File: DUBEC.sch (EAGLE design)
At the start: 69 parts

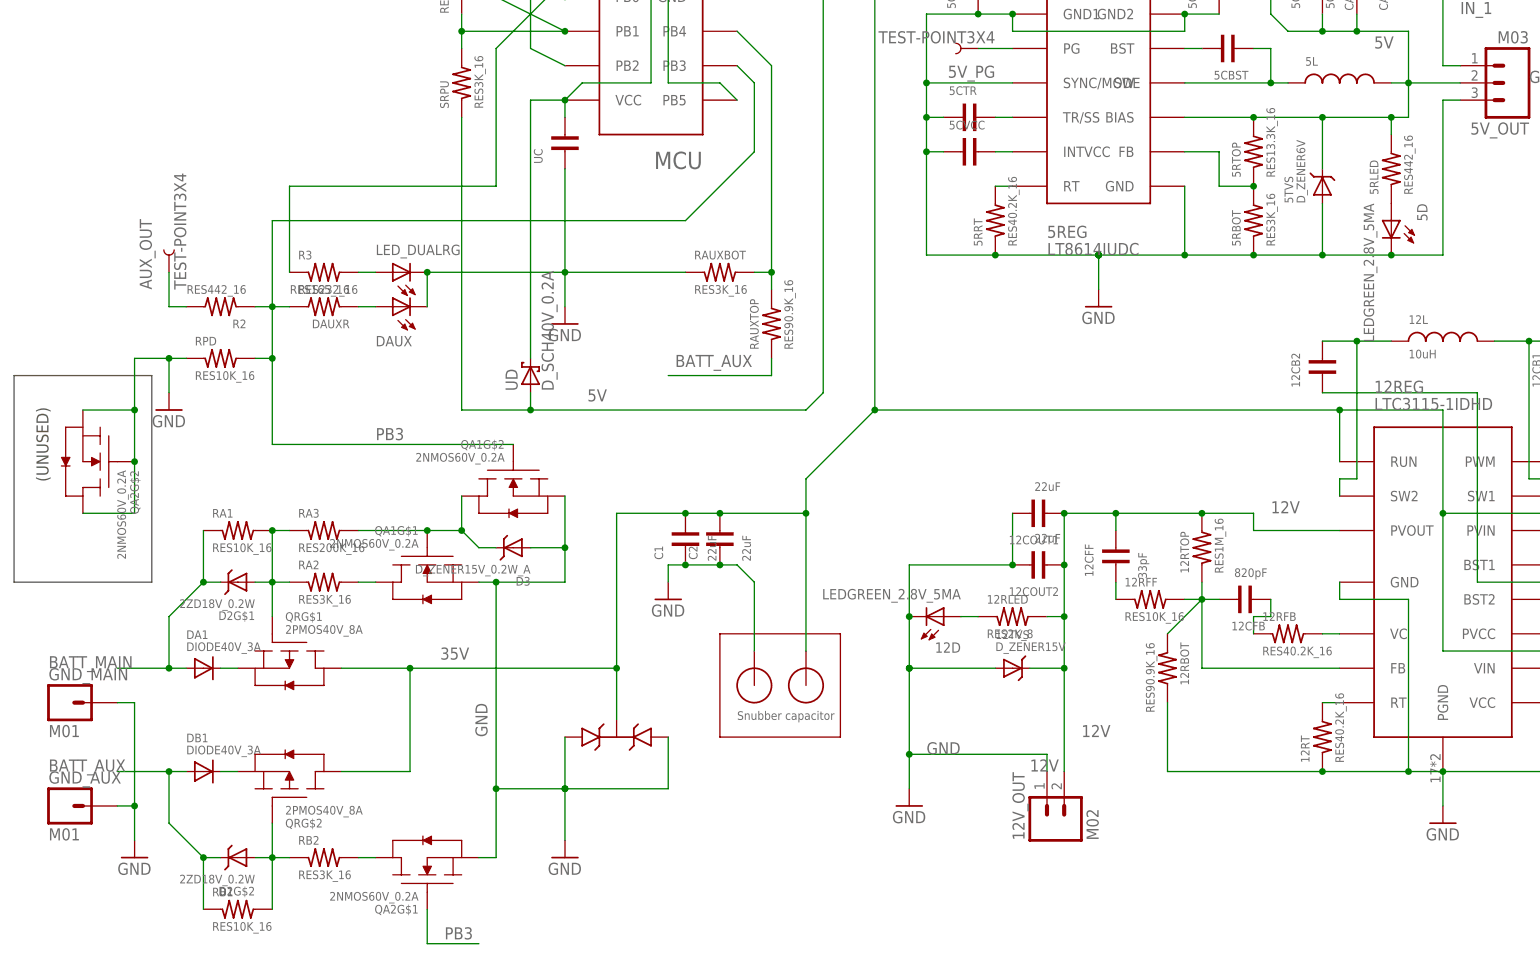
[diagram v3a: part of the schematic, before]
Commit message: Tidying; cap package; LED resistor update
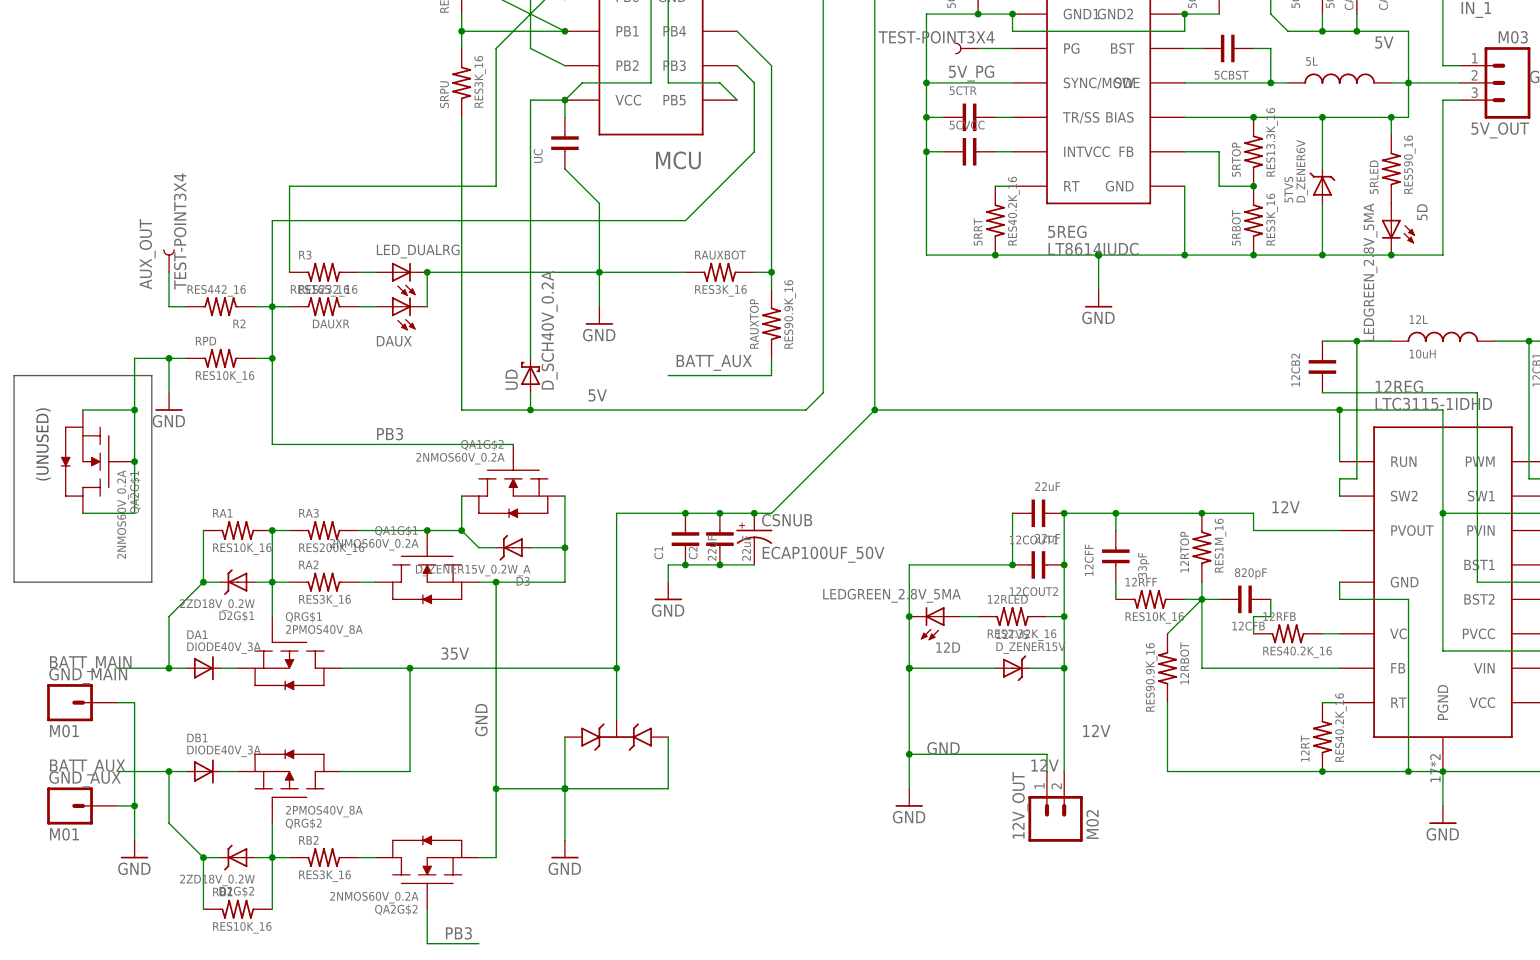
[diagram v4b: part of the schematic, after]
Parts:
- removed CSNUB+, CSNUB-: H10.65MM, dubec:H10.65MM
- added CSNUB: ECAP100UF_50V, dubec:ECAP100UF_50V
- 12RLED: value RES2K_8 -> RES2.32K_16; device dubec:RES2K_8 -> dubec:RES2.32K_16
- 5RLED: value RES442_16 -> RES590_16; device dubec:RES442_16 -> dubec:RES590_16
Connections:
- net 35V: now also CSNUB.+; no longer CSNUB+.1
- net GND: now also CSNUB.-, QA2G$1.D, QA2G$1.G; no longer CSNUB-.1, QA2G$2.D, QA2G$2.G
- net N$10: now also QA2G$2.D; no longer QA2G$1.D
- net PB3: now also QA2G$2.G; no longer QA2G$1.G
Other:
- note removed: "Snubber capacitor"
- moved on the sheet: QA2G$1, QA2G$2
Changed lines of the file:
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@@
 <part name="12D" library="dubec" deviceset="LED" device="GREEN_2.8V_5MA"/>
 <part name="DAUXR" library="dubec" deviceset="RES" device="165_16" value="RES165_16"/>
-<part name="12RLED" library="dubec" deviceset="RES" device="2K_8" value="RES2K_8"/>
-<part name="5RLED" library="dubec" deviceset="RES" device="442_16" value="RES442_16"/>
+<part name="12RLED" library="dubec" deviceset="RES" device="2.32K_16" value="RES2.32K_16"/>
+<part name="5RLED" library="dubec" deviceset="RES" device="590_16" value="RES590_16"/>
 <part name="AVRISP" library="dubec" deviceset="AVRISP" device="H3X2" value="AVRISPH3X2"/>
 <part name="UD" library="dubec" deviceset="D_SCH" device="40V_0.2A" value="D_SCH40V_0.2A"/>
@@
 <part name="R3" library="dubec" deviceset="RES" device="232_16"/>
 <part name="DTVS" library="dubec" deviceset="TVS-SPT" device="36V"/>
-<part name="CSNUB+" library="dubec" deviceset="H1" device="0.65MM"/>
-<part name="CSNUB-" library="dubec" deviceset="H1" device="0.65MM"/>
 <part name="QR" library="dubec" deviceset="2PMOS" device="40V_8A" value="2PMOS40V_8A"/>
 <part name="D2" library="dubec" deviceset="2ZD" device="18V_0.2W" value="2ZD18V_0.2W"/>
@@
 <part name="QA2" library="dubec" deviceset="2NMOS" device="60V_0.2A"/>
 <part name="D3" library="dubec" deviceset="D_ZENER" device="15V_0.2W_A"/>
+<part name="CSNUB" library="dubec" deviceset="ECAP" device="100UF_50V"/>
 </parts>
 <sheets>
 <sheet>
 <plain>
-<wire x1="-30.48" y1="-40.64" x2="-30.48" y2="-55.88" width="0.1524" layer="94"/>
-<wire x1="-30.48" y1="-55.88" x2="-12.7" y2="-55.88" width="0.1524" layer="94"/>
-<wire x1="-12.7" y1="-55.88" x2="-12.7" y2="-40.64" width="0.1524" layer="94"/>
-<wire x1="-12.7" y1="-40.64" x2="-30.48" y2="-40.64" width="0.1524" layer="94"/>
-<text x="-27.94" y="-53.34" size="1.27" layer="95">Snubber capacitor</text>
 <text x="-129.54" y="-12.7" size="1.778" layer="97" rot="R90" align="bottom-center">(UNUSED)</text>
 <wire x1="-134.62" y1="-2.54" x2="-114.3" y2="-2.54" width="0.1524" layer="97"/>
@@
 <instance part="SR1" gate="G$1" x="-68.58" y="55.88" rot="R270"/>
 <instance part="5V_OUT" gate="G$1" x="81.28" y="40.64" rot="R180"/>
-<instance part="GND4" gate="1" x="-53.34" y="5.08"/>
+<instance part="GND4" gate="1" x="-48.26" y="5.08"/>
 <instance part="GND5" gate="1" x="25.4" y="7.62"/>
 <instance part="SRPU" gate="G$1" x="-68.58" y="40.64" rot="R90"/>
@@
 <instance part="R3" gate="G$1" x="-88.9" y="12.7"/>
 <instance part="DTVS" gate="G$1" x="-45.72" y="-55.88"/>
-<instance part="CSNUB+" gate="G$1" x="-17.78" y="-43.18" rot="R270"/>
-<instance part="CSNUB-" gate="G$1" x="-25.4" y="-43.18" rot="R270"/>
 <instance part="QR" gate="G$1" x="-93.98" y="-45.72" rot="R270"/>
 <instance part="QR" gate="G$2" x="-93.98" y="-60.96" rot="MR90"/>
@@
 <instance part="RB1" gate="G$1" x="-101.6" y="-81.28"/>
 <instance part="RA3" gate="G$1" x="-88.9" y="-25.4"/>
-<instance part="QA2" gate="G$1" x="-73.66" y="-73.66" rot="R90"/>
-<instance part="QA2" gate="G$2" x="-124.46" y="-15.24" rot="R180"/>
+<instance part="QA2" gate="G$1" x="-124.46" y="-15.24" rot="R180"/>
+<instance part="QA2" gate="G$2" x="-73.66" y="-73.66" rot="R90"/>
 <instance part="D3" gate="G$1" x="-60.96" y="-27.94" rot="R180"/>
+<instance part="CSNUB" gate="G$1" x="-25.4" y="-25.4"/>
 </instances>
 <busses>
@@
 <wire x1="91.44" y1="-43.18" x2="76.2" y2="-43.18" width="0.1524" layer="91"/>
 <wire x1="76.2" y1="-43.18" x2="76.2" y2="-22.86" width="0.1524" layer="91"/>
-<wire x1="-30.48" y1="-22.86" x2="-17.78" y2="-22.86" width="0.1524" layer="91"/>
-<wire x1="-17.78" y1="-22.86" x2="-17.78" y2="-17.78" width="0.1524" layer="91"/>
-<wire x1="-17.78" y1="-17.78" x2="-7.62" y2="-7.62" width="0.1524" layer="91"/>
+<wire x1="-22.86" y1="-22.86" x2="-7.62" y2="-7.62" width="0.1524" layer="91"/>
 <wire x1="-7.62" y1="-7.62" x2="60.96" y2="-7.62" width="0.1524" layer="91"/>
 <wire x1="60.96" y1="-7.62" x2="76.2" y2="-7.62" width="0.1524" layer="91"/>
@@
 <junction x="-7.62" y="-7.62"/>
 <pinref part="DTVS" gate="G$1" pin="C"/>
-<pinref part="CSNUB+" gate="G$1" pin="1"/>
-<wire x1="-17.78" y1="-22.86" x2="-17.78" y2="-43.18" width="0.1524" layer="91"/>
-<junction x="-17.78" y="-22.86"/>
 <label x="-71.755" y="-44.45" size="1.778" layer="95"/>
 <wire x1="-76.2" y1="-45.72" x2="-45.72" y2="-45.72" width="0.1524" layer="91"/>
@@
 <wire x1="-86.36" y1="-60.96" x2="-76.2" y2="-60.96" width="0.1524" layer="91"/>
 <junction x="-76.2" y="-45.72"/>
+<wire x1="-30.48" y1="-22.86" x2="-25.4" y2="-22.86" width="0.1524" layer="91"/>
+<pinref part="CSNUB" gate="G$1" pin="+"/>
+<wire x1="-25.4" y1="-22.86" x2="-22.86" y2="-22.86" width="0.1524" layer="91"/>
+<junction x="-25.4" y="-22.86"/>
 </segment>
 </net>
@@
 <pinref part="GND4" gate="1" pin="GND"/>
 <pinref part="UC" gate="G$1" pin="1"/>
-<wire x1="-53.34" y1="12.7" x2="-35.56" y2="12.7" width="0.1524" layer="91"/>
-<wire x1="-53.34" y1="27.94" x2="-53.34" y2="12.7" width="0.1524" layer="91"/>
-<junction x="-53.34" y="12.7"/>
-<wire x1="-53.34" y1="7.62" x2="-53.34" y2="12.7" width="0.1524" layer="91"/>
+<wire x1="-48.26" y1="12.7" x2="-35.56" y2="12.7" width="0.1524" layer="91"/>
+<wire x1="-53.34" y1="27.94" x2="-48.26" y2="22.86" width="0.1524" layer="91"/>
+<wire x1="-48.26" y1="22.86" x2="-48.26" y2="12.7" width="0.1524" layer="91"/>
+<junction x="-48.26" y="12.7"/>
+<wire x1="-48.26" y1="7.62" x2="-48.26" y2="12.7" width="0.1524" layer="91"/>
 <pinref part="DAUX" gate="G$1" pin="C2"/>
-<wire x1="-73.66" y1="12.7" x2="-53.34" y2="12.7" width="0.1524" layer="91"/>
+<wire x1="-73.66" y1="12.7" x2="-48.26" y2="12.7" width="0.1524" layer="91"/>
 <pinref part="DAUX" gate="G$1" pin="C1"/>
 <wire x1="-73.66" y1="7.62" x2="-73.66" y2="12.7" width="0.1524" layer="91"/>
@@
 <wire x1="-38.1" y1="-30.48" x2="-38.1" y2="-33.02" width="0.1524" layer="91"/>
 <junction x="-35.56" y="-30.48"/>
-<wire x1="-27.94" y1="-30.48" x2="-30.48" y2="-30.48" width="0.1524" layer="91"/>
 <junction x="-30.48" y="-30.48"/>
-<pinref part="CSNUB-" gate="G$1" pin="1"/>
-<wire x1="-25.4" y1="-43.18" x2="-25.4" y2="-33.02" width="0.1524" layer="91"/>
-<wire x1="-25.4" y1="-33.02" x2="-27.94" y2="-30.48" width="0.1524" layer="91"/>
+<pinref part="CSNUB" gate="G$1" pin="-"/>
+<wire x1="-25.4" y1="-30.48" x2="-30.48" y2="-30.48" width="0.1524" layer="91"/>
 </segment>
 <segment>
@@
 <wire x1="-111.76" y1="-5.08" x2="-111.76" y2="0" width="0.1524" layer="91"/>
 <wire x1="-111.76" y1="0" x2="-109.22" y2="0" width="0.1524" layer="91"/>
-<pinref part="QA2" gate="G$2" pin="D"/>
-<wire x1="-124.46" y1="-22.86" x2="-116.84" y2="-22.86" width="0.1524" layer="91"/>
-<pinref part="QA2" gate="G$2" pin="G"/>
-<wire x1="-116.84" y1="-22.86" x2="-116.84" y2="-15.24" width="0.1524" layer="91"/>
-<wire x1="-116.84" y1="-15.24" x2="-116.84" y2="-7.62" width="0.1524" layer="91"/>
-<junction x="-116.84" y="-15.24"/>
 <wire x1="-116.84" y1="-7.62" x2="-116.84" y2="0" width="0.1524" layer="91"/>
 <wire x1="-116.84" y1="0" x2="-111.76" y2="0" width="0.1524" layer="91"/>
 <junction x="-111.76" y="0"/>
-<pinref part="QA2" gate="G$2" pin="S"/>
+<pinref part="QA2" gate="G$1" pin="S"/>
 <wire x1="-124.46" y1="-7.62" x2="-116.84" y2="-7.62" width="0.1524" layer="91"/>
+<pinref part="QA2" gate="G$1" pin="G"/>
+<wire x1="-116.84" y1="-7.62" x2="-116.84" y2="-15.24" width="0.1524" layer="91"/>
 <junction x="-116.84" y="-7.62"/>
+<wire x1="-116.84" y1="-15.24" x2="-116.84" y2="-22.86" width="0.1524" layer="91"/>
+<junction x="-116.84" y="-15.24"/>
+<pinref part="QA2" gate="G$1" pin="D"/>
+<wire x1="-116.84" y1="-22.86" x2="-124.46" y2="-22.86" width="0.1524" layer="91"/>
 </segment>
 <segment>
@@
 <label x="-64.77" y="-55.88" size="1.778" layer="95" rot="R90"/>
 <pinref part="D3" gate="G$1" pin="A"/>
-<pinref part="QA2" gate="G$1" pin="S"/>
-<wire x1="-66.04" y1="-73.66" x2="-63.5" y2="-73.66" width="0.1524" layer="91"/>
 <pinref part="QA1" gate="G$2" pin="S"/>
 <wire x1="-53.34" y1="-20.32" x2="-53.34" y2="-27.94" width="0.1524" layer="91"/>
 <junction x="-53.34" y="-27.94"/>
+<pinref part="QA2" gate="G$2" pin="S"/>
+<wire x1="-66.04" y1="-73.66" x2="-63.5" y2="-73.66" width="0.1524" layer="91"/>
 </segment>
 </net>
@@
 <label x="-71.12" y="-85.725" size="1.778" layer="95"/>
 <wire x1="-73.66" y1="-86.36" x2="-66.04" y2="-86.36" width="0.1524" layer="91"/>
-<pinref part="QA2" gate="G$1" pin="G"/>
-<wire x1="-73.66" y1="-81.28" x2="-73.66" y2="-86.36" width="0.1524" layer="91"/>
+<pinref part="QA2" gate="G$2" pin="G"/>
+<wire x1="-73.66" y1="-86.36" x2="-73.66" y2="-81.28" width="0.1524" layer="91"/>
 </segment>
 </net>
@@
 <pinref part="DA1" gate="G$1" pin="A"/>
 <wire x1="-119.38" y1="-45.72" x2="-111.76" y2="-45.72" width="0.1524" layer="91"/>
-<label x="-129.54" y="-45.72" size="1.778" layer="95"/>
 <wire x1="-111.76" y1="-45.72" x2="-109.22" y2="-45.72" width="0.1524" layer="91"/>
 <wire x1="-111.76" y1="-45.72" x2="-111.76" y2="-38.1" width="0.1524" layer="91"/>
@@
 <wire x1="-106.68" y1="-25.4" x2="-106.68" y2="-33.02" width="0.1524" layer="91"/>
 <junction x="-106.68" y="-33.02"/>
+<label x="-129.54" y="-45.72" size="1.778" layer="95"/>
 </segment>
 </net>
@@
 <net name="N$10" class="0">
 <segment>
-<pinref part="QA2" gate="G$1" pin="D"/>
 <pinref part="RB2" gate="G$1" pin="2"/>
-<wire x1="-81.28" y1="-73.66" x2="-83.82" y2="-73.66" width="0.1524" layer="91"/>
-</segment>
-</net>
+<pinref part="QA2" gate="G$2" pin="D"/>
+<wire x1="-83.82" y1="-73.66" x2="-81.28" y2="-73.66" width="0.1524" layer="91"/>
+</segment>
+</net>
